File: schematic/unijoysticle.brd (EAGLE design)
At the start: 50.3 x 50.3 mm, 7 parts, among them IC1 4066N, IC2 4066N, IC3 4066N, J1 DB9, J2 DB9, J3 POWER_JACKSLT

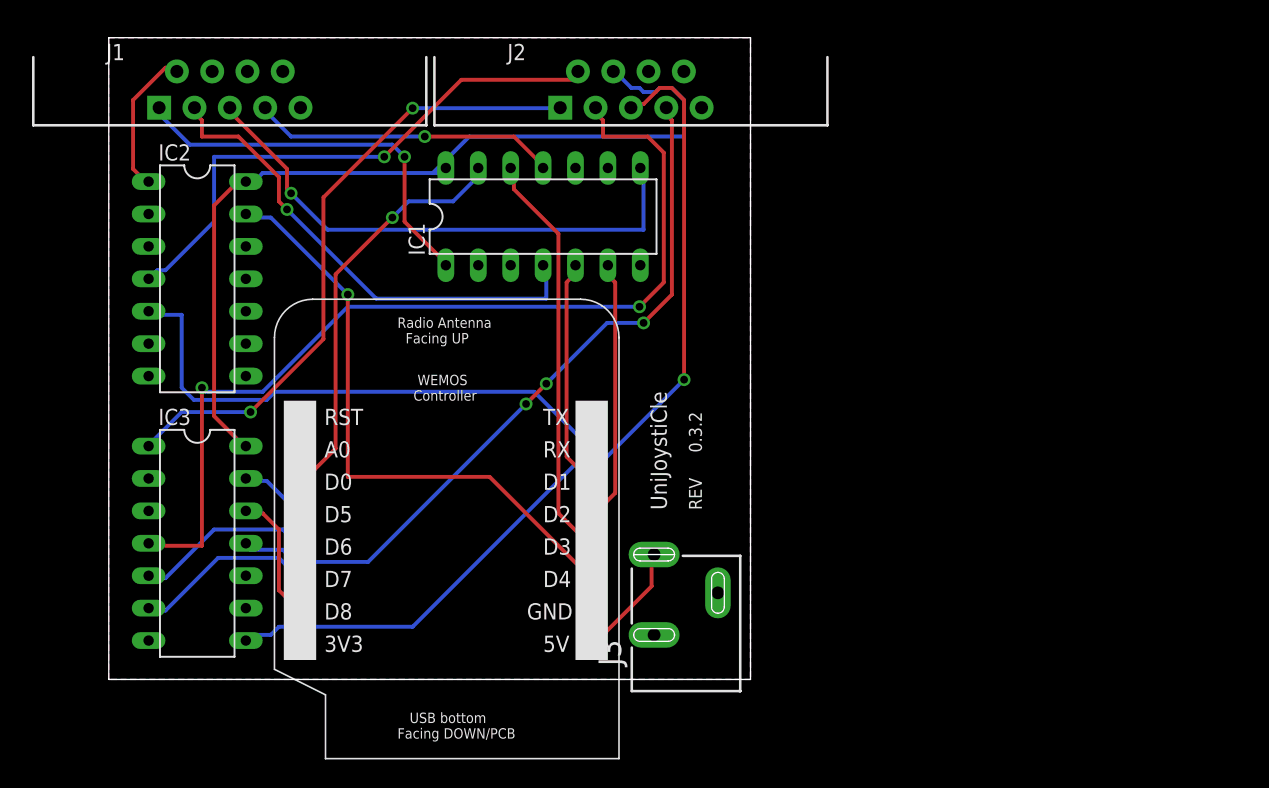
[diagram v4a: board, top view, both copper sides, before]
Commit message: simplified board...
no more barrel jack for the D1 Mini version
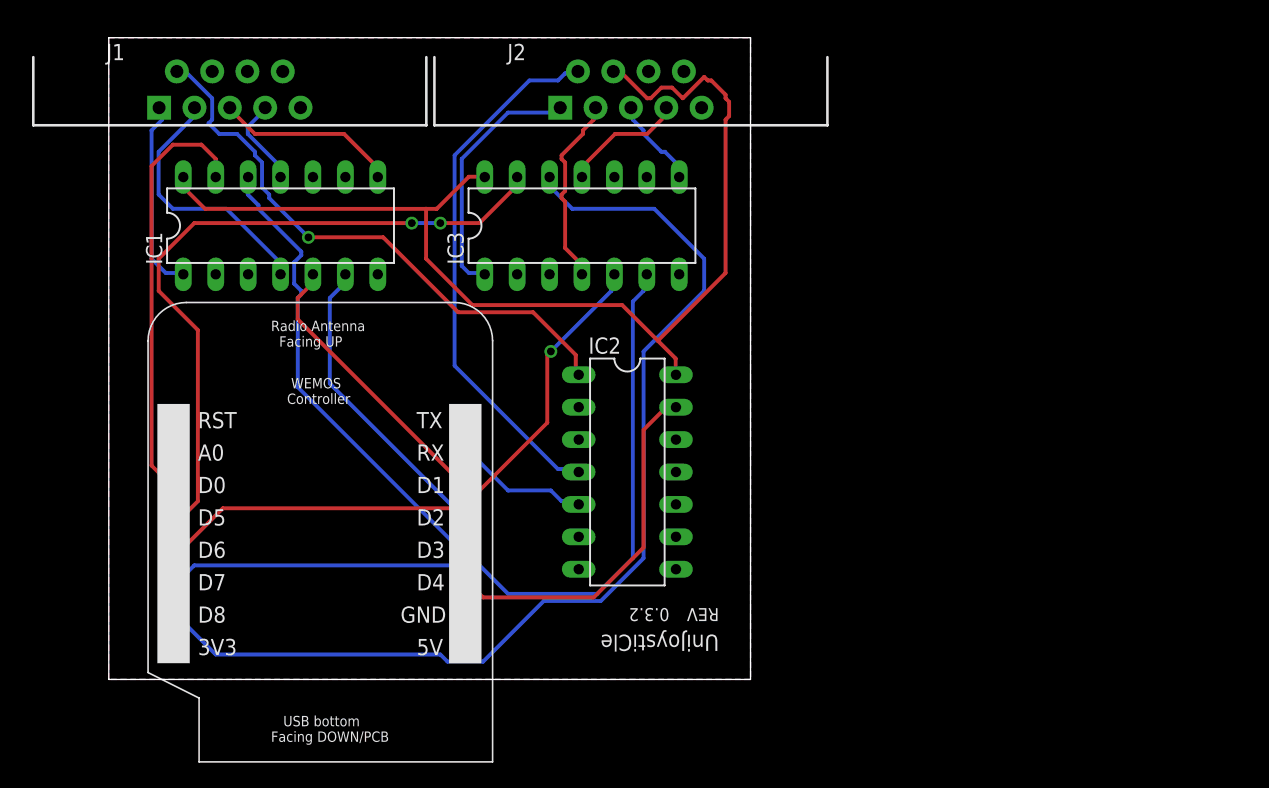
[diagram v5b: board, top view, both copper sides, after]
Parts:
- removed J3: POWER_JACKSLT, SparkFun-Connectors:POWER_JACK_SLOT
- moved IC3 39.1 mm to (37.1, 35.6), turned to 0 degrees
- moved IC2 36.9 mm to (40.6, 16.3)
- moved IC1 20.6 mm to (13.5, 35.6)
- moved U$1 9.91 mm to (5.08, 2.54)
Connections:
- removed net 5V: J3.PWR, U$1.5V
- net GND: no longer J3.GND@1, J3.GND@2
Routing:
- net J2RIGHT: track 10.4 -> 82.3 mm
- net N$15: track 70.1 -> 7.19 mm, vias 1 -> 0
- net N$14: track 74.7 -> 15.1 mm, vias 2 -> 0
- net J2UP: track 5.47 -> 53.8 mm, vias 0 -> 2
- net N$16: track 57.6 -> 9.67 mm, vias 3 -> 0
- net J2LEFT: track 14.4 -> 61.6 mm
- net N$21: track 11.6 -> 45.1 mm, vias 0 -> 1
- net J2DOWN: track 14.1 -> 47.2 mm, vias 0 -> 1
- net J2FIRE: track 43.2 -> 10.7 mm
- net N$13: track 49.8 -> 19.8 mm, vias 2 -> 0
- net N$11: track 42.5 -> 14.4 mm, vias 1 -> 0
- net J1FIRE: track 47.4 -> 28.7 mm, vias 1 -> 0
- net N$10: track 38.8 -> 20.6 mm, vias 1 -> 0
- net VCC: track 69.8 -> 87.5 mm
- net N$12: track 24.2 -> 7.10 mm, vias 1 -> 0
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
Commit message: circular borders
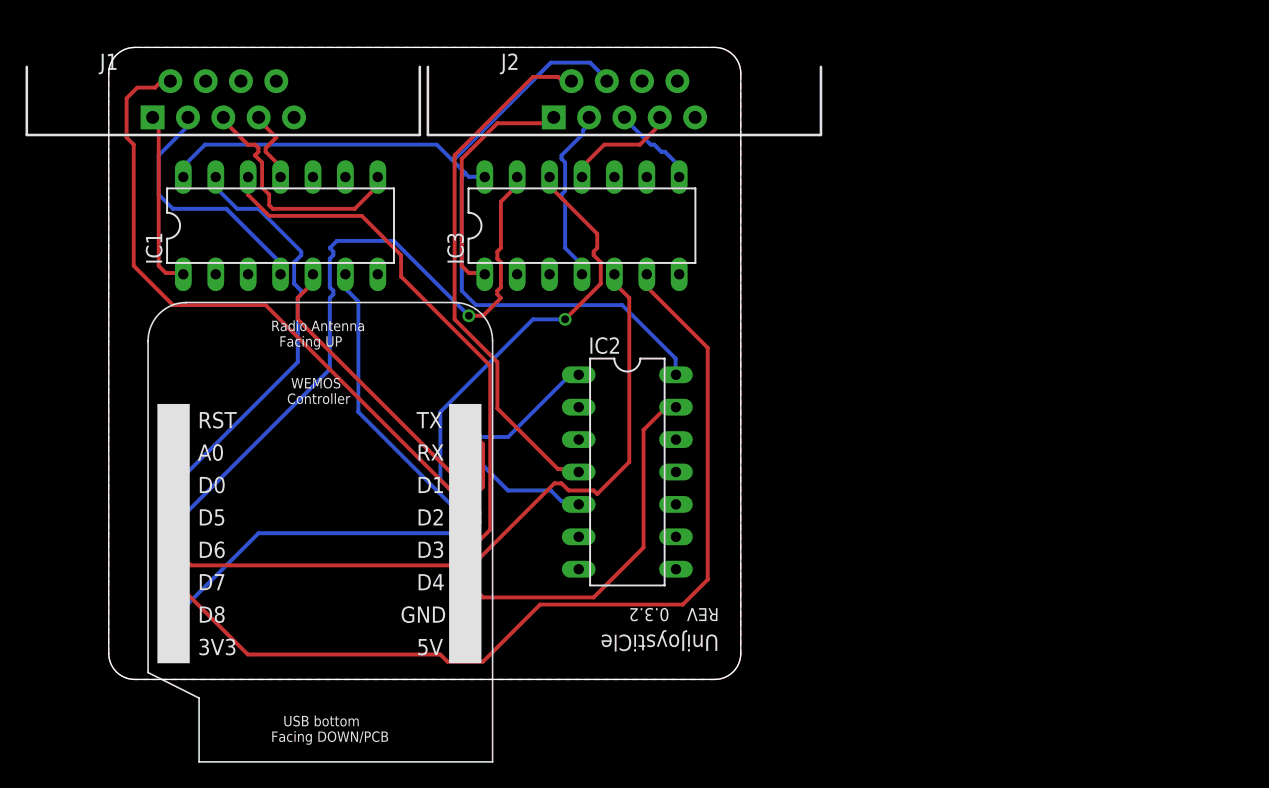
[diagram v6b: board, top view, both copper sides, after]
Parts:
- moved J2 0.92 mm to (40.4, 45.5)
- moved J1 0.92 mm to (8.98, 45.5)
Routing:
- net N$21: track 45.1 -> 67.1 mm
- net J2RIGHT: track 82.3 -> 64.2 mm, vias 0 -> 1
- net VCC: track 87.5 -> 71.9 mm
- net J2LEFT: track 61.6 -> 73.0 mm
- net J2DOWN: track 47.2 -> 55.4 mm, vias 1 -> 0
- net J1RIGHT: track 37.3 -> 42.5 mm
- net N$11: track 14.4 -> 19.0 mm
- net N$9: track 15.3 -> 14.0 mm
- net N$12: track 7.10 -> 6.10 mm
- net J1LEFT: track 24.1 -> 23.1 mm
- net N$10: track 20.6 -> 19.6 mm
- net N$14: track 15.1 -> 14.1 mm
- net J1UP: track 33.5 -> 32.5 mm
- net N$13: track 19.8 -> 19.0 mm
- net N$16: track 9.67 -> 8.85 mm
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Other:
- board size 50.3 x 50.3 mm -> 49.5 x 49.5 mm
